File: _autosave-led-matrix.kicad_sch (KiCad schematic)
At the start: 67 parts, among them U1 MAX7219, U1 Pico

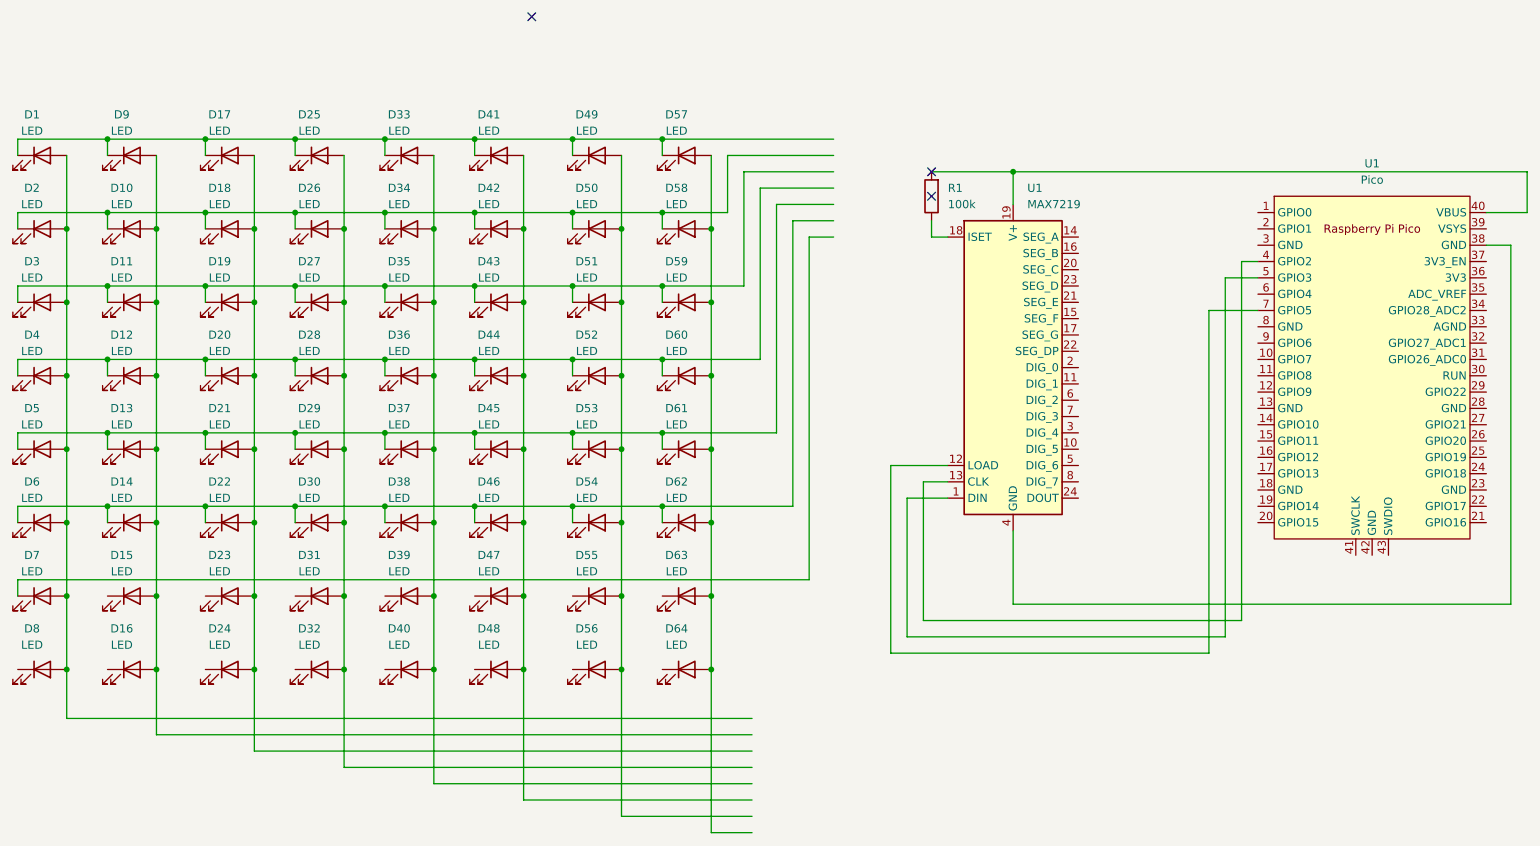
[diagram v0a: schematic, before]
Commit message: chore: connect the matrix to the max7219
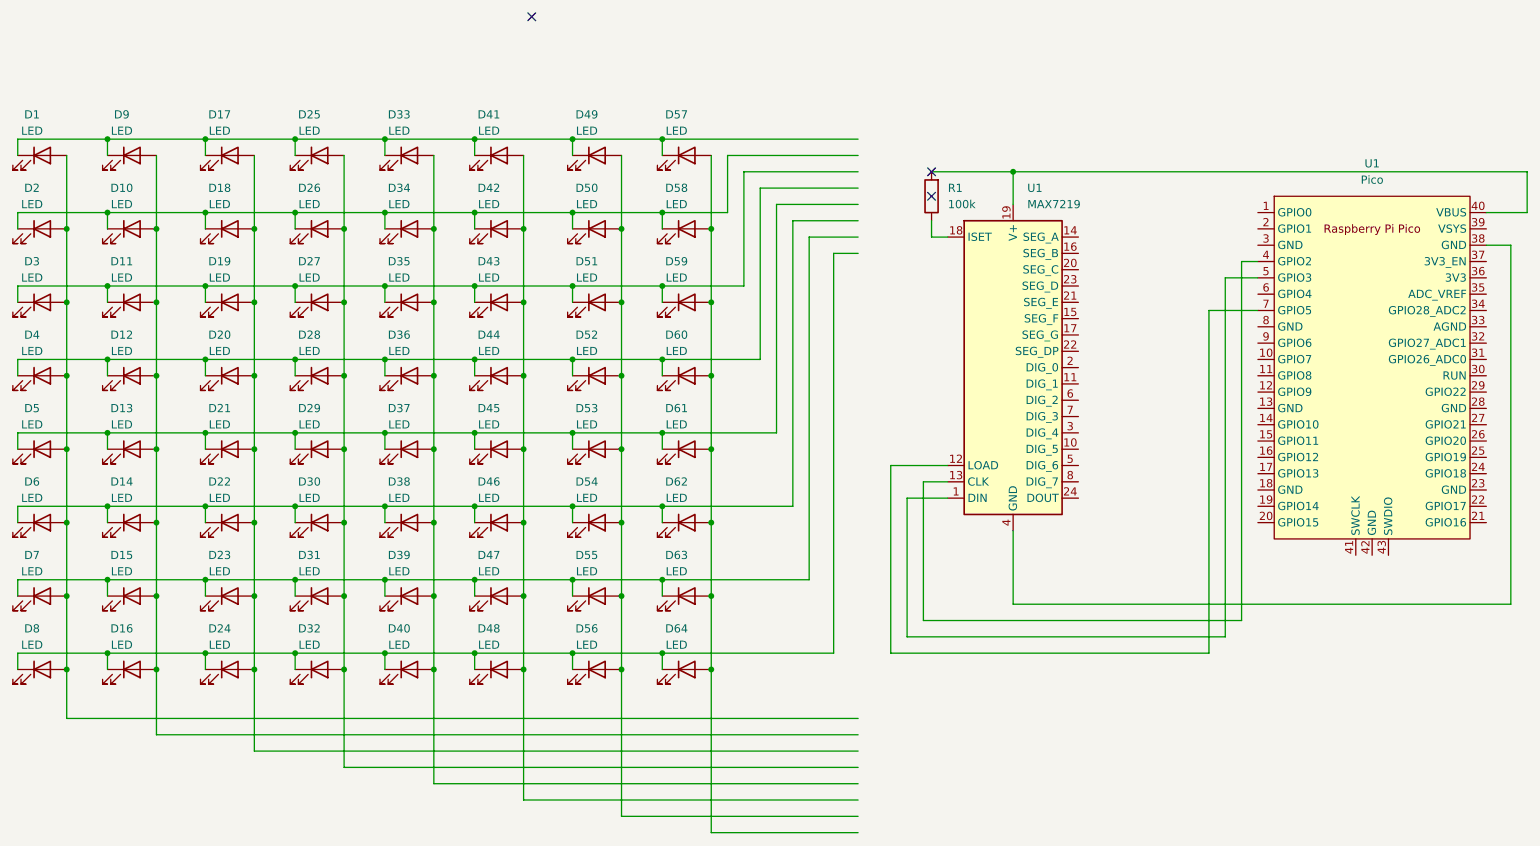
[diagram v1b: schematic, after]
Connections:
- net at D64.1 (K): now also D16.1 (K), D24.1 (K), D32.1 (K), D40.1 (K), D48.1 (K), D56.1 (K), D8.1 (K)
- net at D15.1 (K): now also D23.1 (K), D31.1 (K), D39.1 (K), D47.1 (K), D55.1 (K), D63.1 (K), D7.1 (K)
